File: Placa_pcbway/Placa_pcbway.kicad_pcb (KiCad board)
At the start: 2 copper layers, 100 x 100 mm, 67 parts, among them J1 Molex 0.156, J2 Molex 0.156, J3 Molex 0.156, K1 FINDER-36.11, K2 FINDER-36.11, K3 FINDER-36.11, Q1 2N3904, Q2 2N3904, Q3 2N3904, U1 LM7805_TO220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

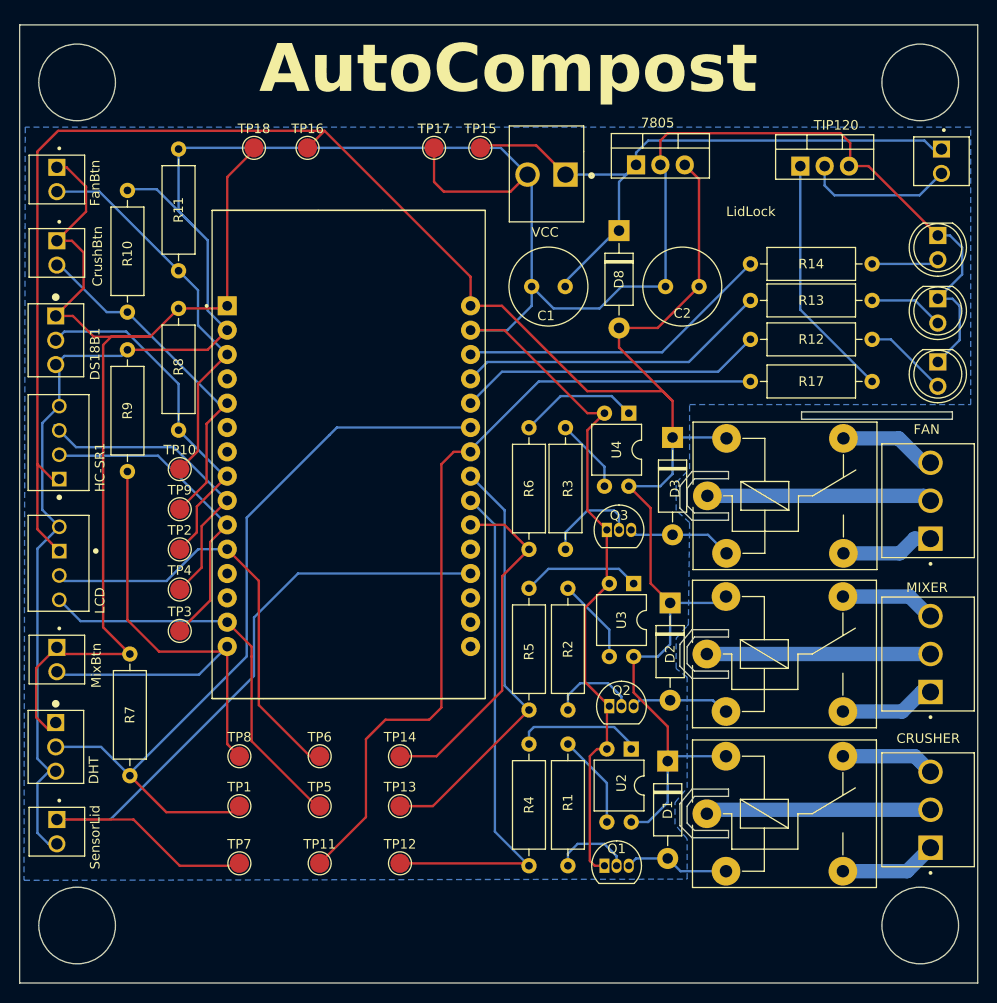
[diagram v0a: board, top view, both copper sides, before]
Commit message: feat: Modificacion de capacitores de 7805
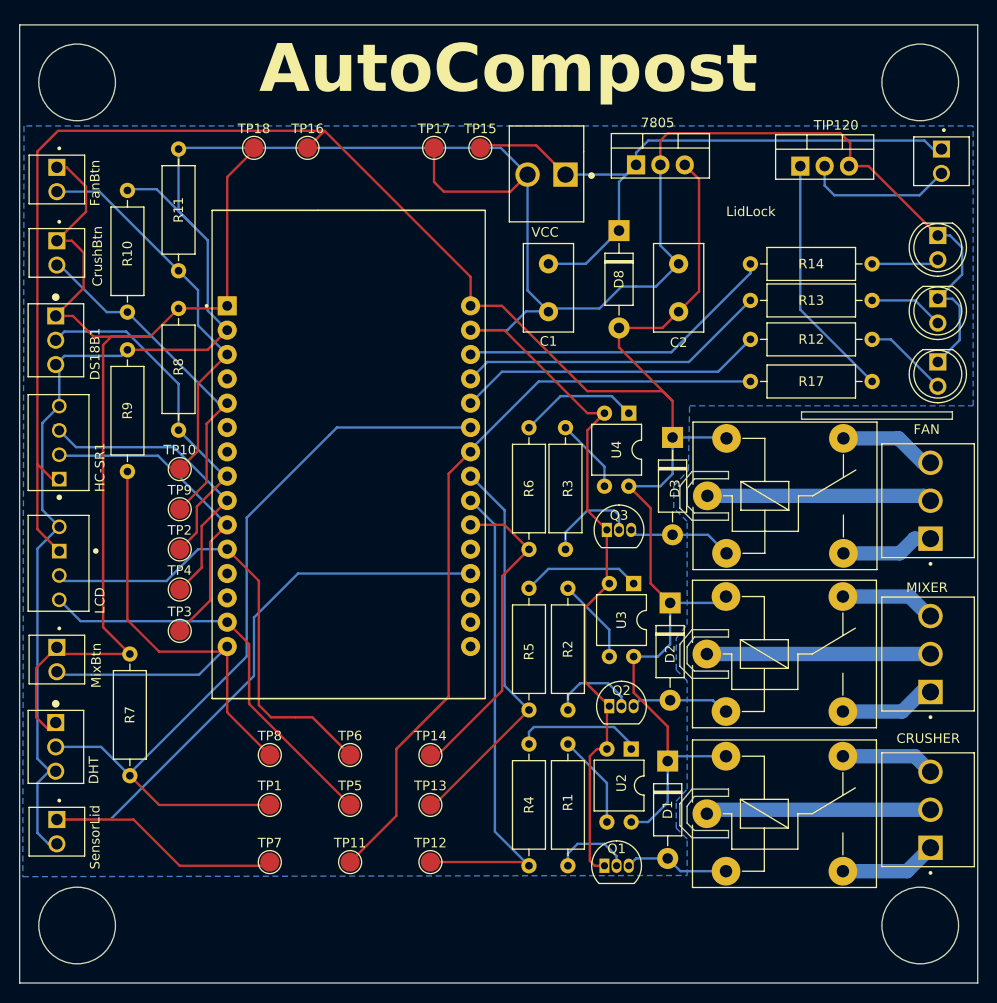
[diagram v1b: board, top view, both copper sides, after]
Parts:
- C1, C2: footprint Capacitor_THT:C_Radial_D8.0mm_H7.0mm_P3.50mm -> Capacitor_THT:C_Disc_D9.0mm_W5.0mm_P5.00mm
- moved C2 3.38 mm to (168.8, 69.9), turned to 90 degrees
- moved TP12 3.18 mm to (142.9, 127.4)
- moved TP13 3.18 mm to (142.9, 121.4)
- moved TP14 3.18 mm to (142.9, 116.2)
- moved TP1 3.18 mm to (126.1, 121.4)
- moved TP7 3.18 mm to (126.1, 127.4)
- moved TP8 3.18 mm to (126.1, 116.2)
- moved TP11 3.18 mm to (134.5, 127.4)
- moved TP5 3.18 mm to (134.5, 121.4)
- moved TP6 3.18 mm to (134.5, 116.2)
- moved C1 2.95 mm to (155.2, 64.9), turned to -90 degrees
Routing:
- net /Lock: track 85.6 -> 80.4 mm
- net /Lid: track 78.4 -> 81.9 mm
- net /Fan: track 36.8 -> 33.6 mm
- net /Mixer: track 44.5 -> 41.3 mm
- net /LCD_SDA: track 45.7 -> 48.9 mm
- net /Crusher: track 54.0 -> 51.1 mm
- net /DHT: track 81.2 -> 84.1 mm
- net /MixerBtn: track 58.0 -> 59.2 mm
- net GND: track 335.6 -> 336.5 mm
- net /LCD_SCL: track 42.2 -> 43.1 mm
- net /VCC: track 68.0 -> 68.8 mm
- net /Led3: track 33.8 -> 34.4 mm
